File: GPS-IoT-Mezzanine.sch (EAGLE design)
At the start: 20 parts, among them J1 F-1X02-SIP-100-40, Q1 DTC143ZEBTL, Q2 DTC143ZEBTL, U1 LD1117D33TR, U2 TXS0104ED

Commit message: Improvements to the mezzanine
added keepout for the antenna, improved silkscreen on top layer, improved poer traces to the Level shifter IC.

Signed off by Thore Krug opensource[at]thorekrug.de
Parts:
- removed CR2032: BS-7, BS-7:BS-7
- removed J1: F-1X02-SIP-100-40, con-headers-jp:F-1X02-SIP-100-40
- added BT1: 6.8MM_COIN_CELL, SparkFun-Batteries:ML414H_IV01E_BATTERY
- added D2: 0.5A/40V/420mV, SparkFun-DiscreteSemi:DIODE-SCHOTTKY-PMEG4005EJ
- added R3: 3.3k, SparkFun-Resistors:3.3KOHM-0603-1/10W-1%
- C8: value 4,7uF -> 1uF
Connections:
- new net N$6: D2.C, R3.2
- net +3V3: now also D2.A
- net GND: now also BT1.-; no longer CR2032.-, J1.1
- net V_BCKP: now also BT1.+, R3.1; no longer CR2032.+, J1.2
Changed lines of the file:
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@@
 <layer number="61" name="stand" color="7" fill="1" visible="no" active="no"/>
 <layer number="70" name="70" color="7" fill="1" visible="no" active="no"/>
+<layer number="88" name="SimResults" color="9" fill="1" visible="yes" active="yes"/>
+<layer number="89" name="SimProbes" color="9" fill="1" visible="yes" active="yes"/>
 <layer number="90" name="Modules" color="5" fill="1" visible="yes" active="yes"/>
 <layer number="91" name="Nets" color="2" fill="1" visible="yes" active="yes"/>
@@
 <layer number="112" name="tSilk" color="7" fill="1" visible="yes" active="yes"/>
 <layer number="113" name="IDFDebug" color="7" fill="1" visible="yes" active="yes"/>
+<layer number="114" name="Badge_Outline" color="7" fill="1" visible="no" active="yes"/>
+<layer number="115" name="ReferenceISLANDS" color="7" fill="1" visible="no" active="yes"/>
 <layer number="116" name="Patch_BOT" color="9" fill="1" visible="yes" active="yes"/>
 <layer number="118" name="Rect_Pads" color="7" fill="1" visible="yes" active="yes"/>
@@
 <part name="SUPPLY7" library="96Boards-IoT-Mezzanine" deviceset="GND" device=""/>
 <part name="SUPPLY8" library="96Boards-IoT-Mezzanine" deviceset="GND" device=""/>
-<part name="CR2032" library="BS-7" deviceset="BS-7" device=""/>
-<part name="SUPPLY9" library="96Boards-IoT-Mezzanine" deviceset="GND" device=""/>
 <part name="LED1" library="led" library_urn="urn:adsk.eagle:library:259" deviceset="LED" device="CHIPLED_1206" package3d_urn="urn:adsk.eagle:package:15823/2"/>
 <part name="C1" library="rcl" library_urn="urn:adsk.eagle:library:334" deviceset="C-EU" device="C0603" package3d_urn="urn:adsk.eagle:package:23616/2" value="100n"/>
@@
 <part name="SUPPLY11" library="96Boards-IoT-Mezzanine" deviceset="GND" device=""/>
 <part name="C7" library="rcl" library_urn="urn:adsk.eagle:library:334" deviceset="C-EU" device="C0603" package3d_urn="urn:adsk.eagle:package:23616/2" value="100n"/>
-<part name="C8" library="rcl" library_urn="urn:adsk.eagle:library:334" deviceset="C-EU" device="C0603" package3d_urn="urn:adsk.eagle:package:23616/2" value="4,7uF"/>
+<part name="C8" library="rcl" library_urn="urn:adsk.eagle:library:334" deviceset="C-EU" device="C0603" package3d_urn="urn:adsk.eagle:package:23616/2" value="1uF"/>
 <part name="SUPPLY12" library="96Boards-IoT-Mezzanine" deviceset="GND" device=""/>
 <part name="SUPPLY13" library="96Boards-IoT-Mezzanine" deviceset="GND" device=""/>
@@
 <part name="R2" library="rcl" library_urn="urn:adsk.eagle:library:334" deviceset="R-EU_" device="R0603" package3d_urn="urn:adsk.eagle:package:23555/3" value="10K"/>
 <part name="SUPPLY20" library="96Boards-IoT-Mezzanine" deviceset="GND" device=""/>
-<part name="J1" library="con-headers-jp" deviceset="F-1X02-" device="SIP-100-40"/>
-<part name="SUPPLY21" library="96Boards-IoT-Mezzanine" deviceset="GND" device=""/>
+<part name="BT1" library="SparkFun-Batteries" deviceset="ML414H_IV01E_BATTERY" device="" value="6.8MM_COIN_CELL"/>
+<part name="D2" library="SparkFun-DiscreteSemi" deviceset="DIODE-SCHOTTKY" device="-PMEG4005EJ" value="0.5A/40V/420mV"/>
+<part name="R3" library="SparkFun-Resistors" deviceset="3.3KOHM" device="-0603-1/10W-1%" value="3.3k"/>
+<part name="SUPPLY22" library="96Boards-IoT-Mezzanine" deviceset="GND" device=""/>
 </parts>
 <sheets>
@@
 <wire x1="-60.96" y1="27.94" x2="-22.86" y2="27.94" width="0.1524" layer="97" style="longdash"/>
 <wire x1="-22.86" y1="27.94" x2="-22.86" y2="106.68" width="0.1524" layer="97" style="longdash"/>
-<text x="-10.16" y="99.06" size="3.81" layer="94">L80-R GPS Module</text>
+<text x="-5.08" y="101.6" size="3.81" layer="94">L80-R GPS Module</text>
 <wire x1="-22.86" y1="27.94" x2="66.04" y2="27.94" width="0.1524" layer="97" style="longdash"/>
 <wire x1="66.04" y1="27.94" x2="127" y2="27.94" width="0.1524" layer="97" style="longdash"/>
@@
 <attribute name="VALUE" x="112.395" y="45.085" size="1.778" layer="96"/>
 </instance>
-<instance part="CR2032" gate="G$1" x="-2.54" y="78.74" smashed="yes" rot="R270">
-<attribute name="NAME" x="1.27" y="82.55" size="1.778" layer="95" rot="R270"/>
-<attribute name="VALUE" x="-7.62" y="82.55" size="1.778" layer="96" rot="R270"/>
-</instance>
-<instance part="SUPPLY9" gate="GND" x="-2.54" y="63.5" smashed="yes">
-<attribute name="VALUE" x="-4.445" y="60.325" size="1.778" layer="96"/>
-</instance>
 <instance part="LED1" gate="G$1" x="114.3" y="78.74" smashed="yes">
 <attribute name="NAME" x="117.856" y="74.168" size="1.778" layer="95" rot="R90"/>
@@
 <attribute name="VALUE" x="-111.125" y="-59.055" size="1.778" layer="96"/>
 </instance>
-<instance part="J1" gate="G$1" x="55.88" y="53.34" smashed="yes" rot="MR180">
-<attribute name="VALUE" x="54.61" y="60.96" size="1.27" layer="96" rot="MR180"/>
-<attribute name="NAME" x="54.61" y="50.038" size="1.778" layer="95" rot="MR180"/>
-</instance>
-<instance part="SUPPLY21" gate="GND" x="43.18" y="48.26" smashed="yes">
-<attribute name="VALUE" x="41.275" y="45.085" size="1.778" layer="96"/>
+<instance part="BT1" gate="G$1" x="-15.24" y="71.12" smashed="yes" rot="R270">
+<attribute name="NAME" x="-12.7" y="73.406" size="1.778" layer="95" font="vector" rot="MR0" align="bottom-center"/>
+</instance>
+<instance part="D2" gate="G$1" x="-15.24" y="96.52" smashed="yes" rot="R270">
+<attribute name="NAME" x="-12.7" y="98.552" size="1.778" layer="95" font="vector"/>
+<attribute name="VALUE" x="-12.7" y="97.028" size="1.778" layer="96" font="vector" align="top-left"/>
+</instance>
+<instance part="R3" gate="G$1" x="-15.24" y="86.36" smashed="yes" rot="R90">
+<attribute name="NAME" x="-16.764" y="86.36" size="1.778" layer="95" font="vector" rot="R90" align="bottom-center"/>
+<attribute name="VALUE" x="-13.716" y="86.36" size="1.778" layer="96" font="vector" rot="R90" align="top-center"/>
+</instance>
+<instance part="SUPPLY22" gate="GND" x="-15.24" y="60.96" smashed="yes">
+<attribute name="VALUE" x="-17.145" y="57.785" size="1.778" layer="96"/>
 </instance>
 </instances>
@@
 </segment>
 <segment>
-<pinref part="SUPPLY9" gate="GND" pin="GND"/>
-<pinref part="CR2032" gate="G$1" pin="-"/>
-<wire x1="-2.54" y1="66.04" x2="-2.54" y2="71.12" width="0.1524" layer="91"/>
-</segment>
-<segment>
 <pinref part="U1" gate="G$1" pin="GND"/>
 <wire x1="-81.28" y1="5.08" x2="-78.74" y2="5.08" width="0.1524" layer="91"/>
@@
 </segment>
 <segment>
-<pinref part="SUPPLY21" gate="GND" pin="GND"/>
-<wire x1="43.18" y1="50.8" x2="43.18" y2="53.34" width="0.1524" layer="91"/>
-<pinref part="J1" gate="G$1" pin="1"/>
-<wire x1="43.18" y1="53.34" x2="50.8" y2="53.34" width="0.1524" layer="91"/>
+<pinref part="BT1" gate="G$1" pin="-"/>
+<wire x1="-15.24" y1="66.04" x2="-15.24" y2="63.5" width="0.1524" layer="91"/>
+<pinref part="SUPPLY22" gate="GND" pin="GND"/>
 </segment>
 </net>
@@
 <label x="106.68" y="99.06" size="1.778" layer="95"/>
 </segment>
+<segment>
+<pinref part="D2" gate="G$1" pin="A"/>
+<wire x1="-15.24" y1="101.6" x2="-15.24" y2="99.06" width="0.1524" layer="91"/>
+<label x="-15.24" y="101.6" size="1.27" layer="95" rot="R180" xref="yes"/>
+</segment>
 </net>
 <net name="V_BCKP" class="0">
-<segment>
-<pinref part="L80-R" gate="G$1" pin="V_BCKP"/>
-<label x="2.54" y="91.44" size="1.27" layer="95"/>
-<pinref part="CR2032" gate="G$1" pin="+"/>
-<wire x1="-2.54" y1="86.36" x2="-2.54" y2="91.44" width="0.1524" layer="91"/>
-<wire x1="-2.54" y1="91.44" x2="12.7" y2="91.44" width="0.1524" layer="91"/>
-</segment>
 <segment>
 <pinref part="C7" gate="G$1" pin="1"/>
@@
 </segment>
 <segment>
-<label x="40.64" y="55.88" size="1.27" layer="95"/>
-<pinref part="J1" gate="G$1" pin="2"/>
-<wire x1="48.26" y1="55.88" x2="50.8" y2="55.88" width="0.1524" layer="91"/>
+<pinref part="BT1" gate="G$1" pin="+"/>
+<wire x1="0" y1="78.74" x2="-15.24" y2="78.74" width="0.1524" layer="91"/>
+<wire x1="-15.24" y1="78.74" x2="-15.24" y2="76.2" width="0.1524" layer="91"/>
+<pinref part="R3" gate="G$1" pin="1"/>
+<wire x1="-15.24" y1="81.28" x2="-15.24" y2="78.74" width="0.1524" layer="91"/>
+<junction x="-15.24" y="78.74"/>
+<label x="5.08" y="78.74" size="1.27" layer="95" xref="yes"/>
+<pinref part="L80-R" gate="G$1" pin="V_BCKP"/>
+<wire x1="12.7" y1="91.44" x2="0" y2="91.44" width="0.1524" layer="91"/>
+<wire x1="0" y1="91.44" x2="0" y2="78.74" width="0.1524" layer="91"/>
 </segment>
 </net>
@@
 </segment>
 </net>
+<net name="N$6" class="0">
+<segment>
+<pinref part="D2" gate="G$1" pin="C"/>
+<pinref part="R3" gate="G$1" pin="2"/>
+<wire x1="-15.24" y1="93.98" x2="-15.24" y2="91.44" width="0.1524" layer="91"/>
+</segment>
+</net>

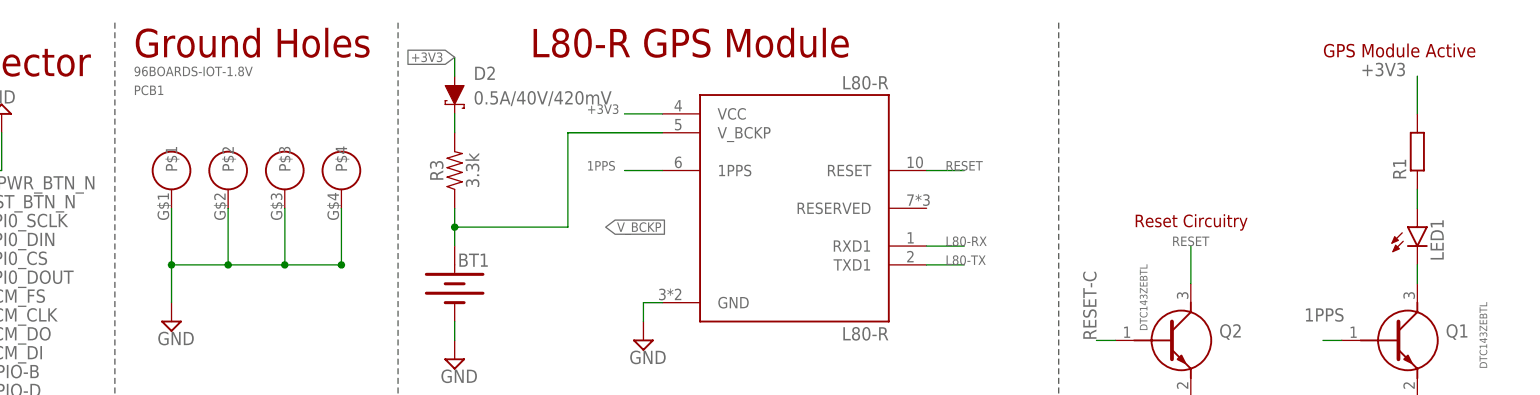
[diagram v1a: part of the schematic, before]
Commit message: Board Update + BOM
Added Round Corner to make the Board more pleasing to the eye, added current limiting resistor for the pink status LED indication 1PPS ( 1 Puls per Second ) created by the L80-R GPS Module. Added BOM ( Bill of material ) in CSV format in the folder misc. Added Missing Datasheets.

Signed off by: Thore Krug opensource[at]thorekrug.de
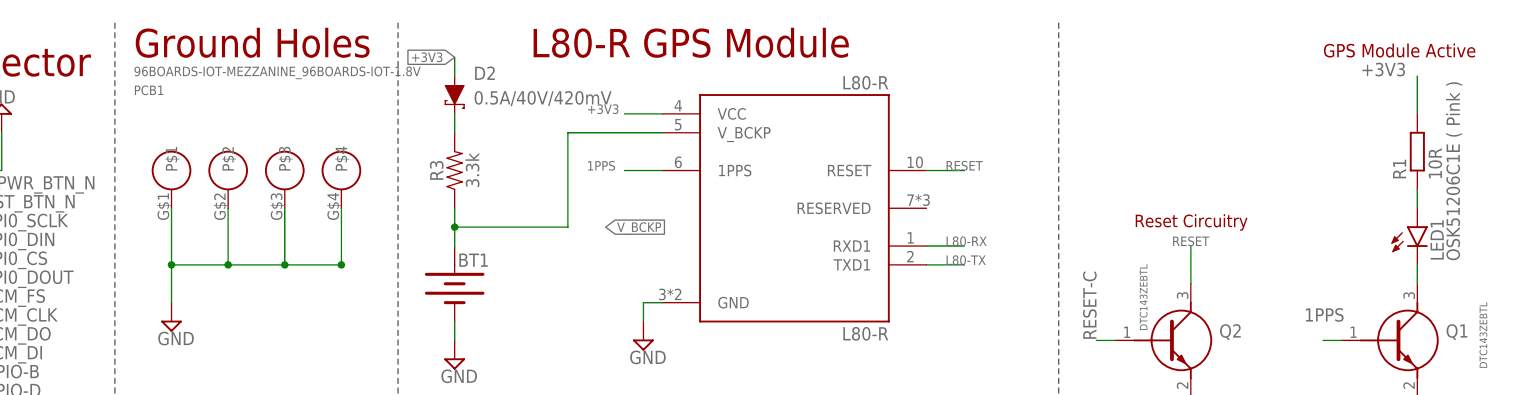
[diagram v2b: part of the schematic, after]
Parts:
- LED1: value (none) -> OSK51206C1E ( Pink )
- PCB1: value 96BOARDS-IOT-1.8V -> 96BOARDS-IOT-MEZZANINE_96BOARDS-IOT-1.8V; device 96Boards-IoT-Mezzanine:96BOARDS-IOT-1.8V -> GPS-IoT-Mezzanine:96BOARDS-IOT-MEZZANINE_96BOARDS-IOT-1.8V
- R1: value (none) -> 10R
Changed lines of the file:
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@@
 <layer number="40" name="bKeepout" color="1" fill="11" visible="no" active="no"/>
 <layer number="41" name="tRestrict" color="4" fill="10" visible="no" active="no"/>
-<layer number="42" name="bRestrict" color="1" fill="10" visible="no" active="no"/>
+<layer number="42" name="bRestrict" color="1" fill="3" visible="no" active="no"/>
 <layer number="43" name="vRestrict" color="2" fill="10" visible="no" active="no"/>
 <layer number="44" name="Drills" color="7" fill="1" visible="no" active="no"/>
@@
 <classes>
 <class number="0" name="default" width="0" drill="0">
+<clearance class="0" value="0.205"/>
 </class>
 <class number="3" name="power" width="0" drill="0">
@@
 </classes>
 <parts>
-<part name="FRAME3" library="frames" deviceset="A4L-LOC" device=""/>
-<part name="PCB1" library="96Boards-IoT-Mezzanine" deviceset="96BOARDS-IOT-1.8V" device=""/>
+<part name="FRAME3" library="frames" library_urn="urn:adsk.eagle:library:229" deviceset="A4L-LOC" device=""/>
+<part name="PCB1" library="GPS-IoT-Mezzanine" deviceset="96BOARDS-IOT-MEZZANINE_96BOARDS-IOT-1.8V" device=""/>
 <part name="SUPPLY4" library="96Boards-IoT-Mezzanine" deviceset="GND" device=""/>
 <part name="U$1" library="96Boards-IoT-Mezzanine" deviceset="57202-G52-20LF" device=""/>
@@
 <part name="SUPPLY7" library="96Boards-IoT-Mezzanine" deviceset="GND" device=""/>
 <part name="SUPPLY8" library="96Boards-IoT-Mezzanine" deviceset="GND" device=""/>
-<part name="LED1" library="led" library_urn="urn:adsk.eagle:library:259" deviceset="LED" device="CHIPLED_1206" package3d_urn="urn:adsk.eagle:package:15823/2"/>
+<part name="LED1" library="led" library_urn="urn:adsk.eagle:library:259" deviceset="LED" device="CHIPLED_1206" package3d_urn="urn:adsk.eagle:package:15823/2" value="OSK51206C1E ( Pink ) "/>
 <part name="C1" library="rcl" library_urn="urn:adsk.eagle:library:334" deviceset="C-EU" device="C0603" package3d_urn="urn:adsk.eagle:package:23616/2" value="100n"/>
 <part name="C2" library="rcl" library_urn="urn:adsk.eagle:library:334" deviceset="C-EU" device="C0603" package3d_urn="urn:adsk.eagle:package:23616/2" value="10uF"/>
@@
 <part name="C5" library="rcl" library_urn="urn:adsk.eagle:library:334" deviceset="C-EU" device="C0603" package3d_urn="urn:adsk.eagle:package:23616/2" value="10uF"/>
 <part name="C6" library="rcl" library_urn="urn:adsk.eagle:library:334" deviceset="C-EU" device="C0603" package3d_urn="urn:adsk.eagle:package:23616/2" value="100n"/>
-<part name="R1" library="rcl" library_urn="urn:adsk.eagle:library:334" deviceset="R-EU_" device="R1206" package3d_urn="urn:adsk.eagle:package:23540/2"/>
+<part name="R1" library="rcl" library_urn="urn:adsk.eagle:library:334" deviceset="R-EU_" device="R1206" package3d_urn="urn:adsk.eagle:package:23540/2" value="10R"/>
 <part name="U1" library="LD1117D33TR" deviceset="LD1117D33TR" device=""/>
 <part name="U2" library="TXS0104ED" deviceset="TXS0104ED" device=""/>
